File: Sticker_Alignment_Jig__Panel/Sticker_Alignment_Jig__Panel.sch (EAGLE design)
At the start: 6 parts

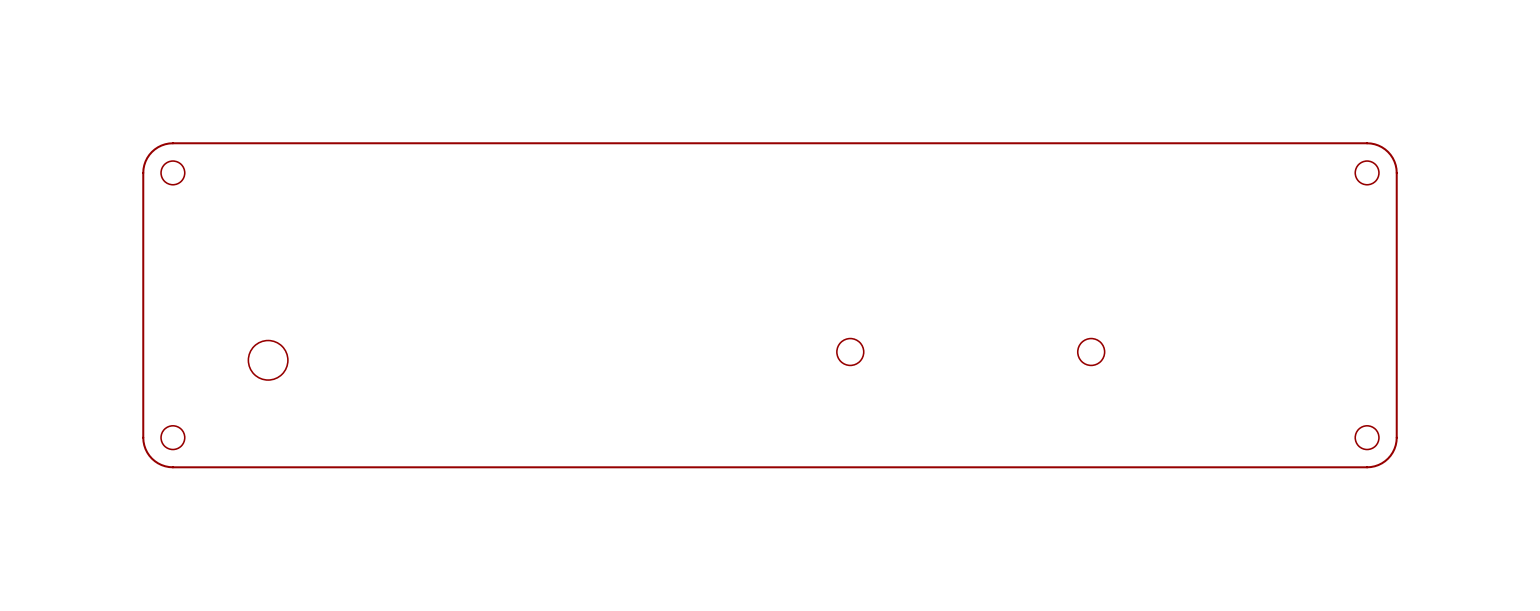
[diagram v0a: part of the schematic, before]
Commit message: Update sticker alignment jig
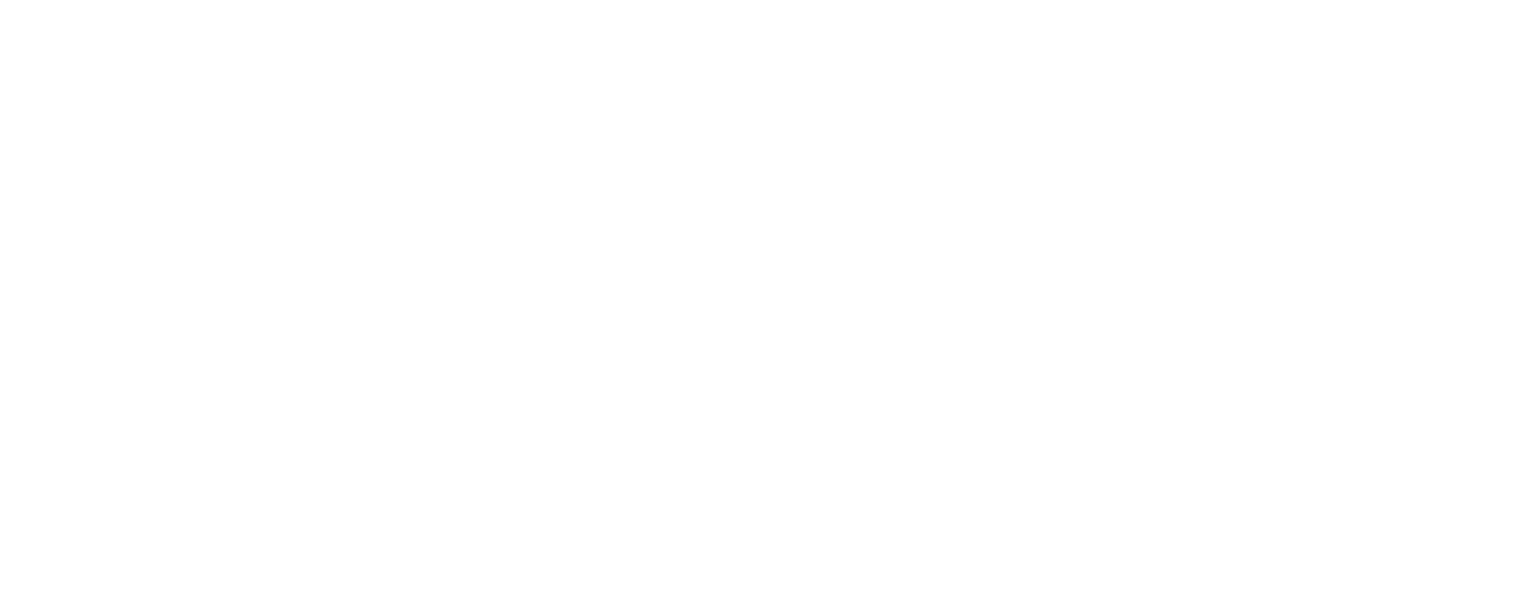
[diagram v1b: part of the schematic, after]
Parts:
- removed U$13, U$14: BUTTON, CORS_Panels:BUTTON
- removed U$2: PANEL_OUTLINE, CORS_Panels:PANEL_OUTLINE
- removed U$3: LED, CORS_Panels:LED
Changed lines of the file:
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@@
 <part name="LOGO1" library="SparkFun-Aesthetics" deviceset="SFE_LOGO_NAME_FLAME" device=".3_INCH" value="SFE_LOGO_NAME_FLAME.3_INCH"/>
 <part name="FRAME1" library="SparkFun-Aesthetics" deviceset="FRAME-LETTER" device=""/>
-<part name="U$2" library="CORS_Panels" deviceset="PANEL_OUTLINE" device=""/>
-<part name="U$3" library="CORS_Panels" deviceset="LED" device=""/>
-<part name="U$13" library="CORS_Panels" deviceset="BUTTON" device=""/>
-<part name="U$14" library="CORS_Panels" deviceset="BUTTON" device=""/>
 </parts>
 <sheets>
@@
 <attribute name="REV" x="236.22" y="6.604" size="2.7432" layer="94" font="vector"/>
 </instance>
-<instance part="U$2" gate="G$1" x="127" y="93.98" smashed="yes"/>
-<instance part="U$3" gate="G$1" x="63.5" y="96.52" smashed="yes"/>
-<instance part="U$13" gate="G$1" x="167.64" y="96.52" smashed="yes"/>
-<instance part="U$14" gate="G$1" x="137.16" y="96.52" smashed="yes"/>
 </instances>
 <busses>
